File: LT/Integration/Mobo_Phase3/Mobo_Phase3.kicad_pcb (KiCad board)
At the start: 4 copper layers, 90.2 x 95.9 mm, 70 parts, among them J1 Bus, J2 Conn_Coaxial, J3 Conn_Coaxial, J4 Conn_Coaxial, J6 Conn_Coaxial, J7 Conn_Coaxial, Q1 2N5486, U1 BAP64Q

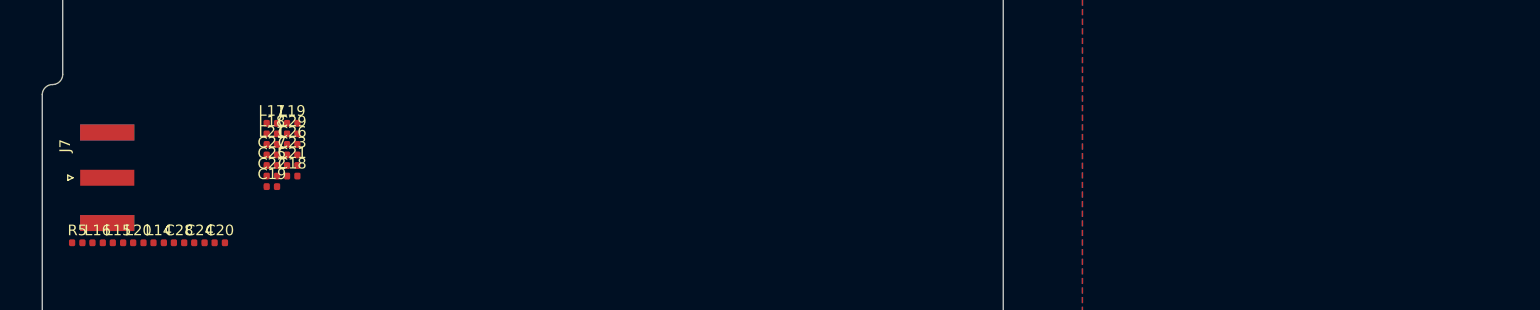
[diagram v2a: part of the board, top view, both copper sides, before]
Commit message: Finished PA Schematic Layout with footprints associated with it
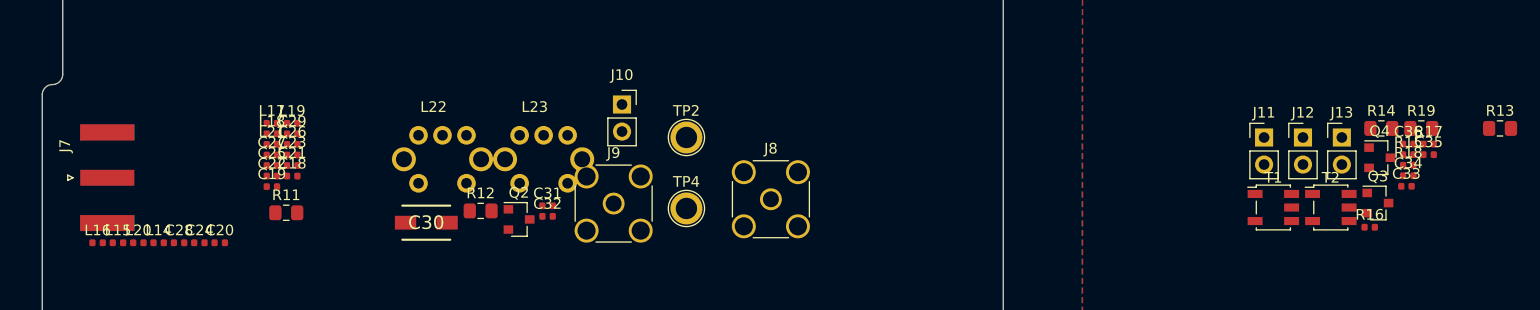
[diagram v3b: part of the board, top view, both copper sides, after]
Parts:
- removed R5: 0 Ohms, Resistor_SMD:R_0402_1005Metric
- added C30: C_Variable, LT:CAP_trimmer_SGC3_Download, F.Cu at (164.5, 107.6)
- added C31: 1uF, Capacitor_SMD:C_0402_1005Metric, F.Cu at (175.9, 106.0)
- added C32: 1uF, Capacitor_SMD:C_0402_1005Metric, F.Cu at (175.9, 107.0)
- added C33: 100nF, Capacitor_SMD:C_0402_1005Metric, F.Cu at (256.5, 104.2)
- added C34: 100nF, Capacitor_SMD:C_0402_1005Metric, F.Cu at (256.7, 103.2)
- added C35: 100nF, Capacitor_SMD:C_0402_1005Metric, F.Cu at (258.6, 101.2)
- added C36: 100nF, Capacitor_SMD:C_0402_1005Metric, F.Cu at (256.7, 100.2)
- added J10: Conn_01x02_Female, Connector_PinSocket_2.54mm:PinSocket_1x02_P2.54mm_Vertical, F.Cu at (182.9, 96.5)
- added J11: Conn_01x02_Male, Connector_PinHeader_2.54mm:PinHeader_1x02_P2.54mm_Vertical, F.Cu at (243.1, 99.6)
- added J12: Conn_01x02_Male, Connector_PinHeader_2.54mm:PinHeader_1x02_P2.54mm_Vertical, F.Cu at (246.8, 99.6)
- added J13: Conn_01x02_Male, Connector_PinHeader_2.54mm:PinHeader_1x02_P2.54mm_Vertical, F.Cu at (250.4, 99.6)
- added J8: Conn_Coaxial, Connector_Coaxial:SMA_Amphenol_132291_Vertical, F.Cu at (196.8, 105.4)
- added J9: Conn_Coaxial, Connector_Coaxial:SMA_Amphenol_132291_Vertical, F.Cu at (182.1, 105.8)
- added L22: LTRIM, LT:IND_trimmer_7M3, F.Cu at (166.0, 101.7)
- added L23: LTRIM, LT:IND_trimmer_7M3, F.Cu at (175.5, 101.7)
- added Q2: Q_NJFET_DSG, Package_TO_SOT_SMD:SOT-23, F.Cu at (173.2, 107.3)
- added Q3: Q_NPN_BEC, Package_TO_SOT_SMD:SOT-23, F.Cu at (253.8, 105.8)
- added Q4: Q_PNP_BEC, Package_TO_SOT_SMD:SOT-23, F.Cu at (254.0, 101.5)
- added R11: 0, Resistor_SMD:R_0805_2012Metric_Pad1.15x1.40mm_HandSolder, F.Cu at (151.4, 106.7)
- added R12: 0, Resistor_SMD:R_0805_2012Metric_Pad1.15x1.40mm_HandSolder, F.Cu at (169.6, 106.5)
- added R13: 0, Resistor_SMD:R_0805_2012Metric_Pad1.15x1.40mm_HandSolder, F.Cu at (265.3, 98.8)
- added R14: 0, Resistor_SMD:R_0805_2012Metric_Pad1.15x1.40mm_HandSolder, F.Cu at (254.1, 98.8)
- added R15: 33k, Resistor_SMD:R_0402_1005Metric, F.Cu at (256.7, 101.2)
- added R16: 47k, Resistor_SMD:R_0402_1005Metric, F.Cu at (253.0, 108.0)
- added R17: 33k, Resistor_SMD:R_0402_1005Metric, F.Cu at (258.6, 100.2)
- added R18: 47k, Resistor_SMD:R_0402_1005Metric, F.Cu at (256.7, 102.2)
- added R19: 0, Resistor_SMD:R_0805_2012Metric_Pad1.15x1.40mm_HandSolder, F.Cu at (257.9, 98.8)
- added T1: Transformer_1P_SS, Transformer_SMD:Transformer_MACOM_SM-22, F.Cu at (244.0, 106.2)
- added T2: Transformer_1P_SS, Transformer_SMD:Transformer_MACOM_SM-22, F.Cu at (249.4, 106.2)
- added TP2: TestPoint_Probe, TestPoint:TestPoint_Plated_Hole_D2.0mm, F.Cu at (188.9, 99.6)
- added TP4: TestPoint_Probe, TestPoint:TestPoint_Plated_Hole_D2.0mm, F.Cu at (188.9, 106.3)
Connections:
- net Net-(C18-Pad1) renamed /29.4 MHz Bandpass Filter/29.4BPF_IN
- C29 pad 1: Net-(C29-Pad1) -> /29.4 MHz Bandpass Filter/29.4BPF_OUT
- J1 pad 1: (no net) -> Net-(J1-Pad1)
- J1 pad 10: (no net) -> Net-(J1-Pad10)
- J1 pad 100: (no net) -> Net-(J1-Pad100)
- J1 pad 101: (no net) -> Net-(J1-Pad101)
- J1 pad 102: (no net) -> Net-(J1-Pad102)
- J1 pad 103: (no net) -> Net-(J1-Pad103)
- J1 pad 104: (no net) -> Net-(J1-Pad104)
- J1 pad 105: (no net) -> Net-(J1-Pad105)
- J1 pad 106: (no net) -> Net-(J1-Pad106)
- J1 pad 107: (no net) -> Net-(J1-Pad107)
- J1 pad 108: (no net) -> Net-(J1-Pad108)
- J1 pad 109: (no net) -> Net-(J1-Pad109)
- J1 pad 11: (no net) -> Net-(J1-Pad11)
- J1 pad 110: (no net) -> Net-(J1-Pad110)
- J1 pad 111: (no net) -> Net-(J1-Pad111)
- J1 pad 112: (no net) -> Net-(J1-Pad112)
- J1 pad 113: (no net) -> Net-(J1-Pad113)
- J1 pad 114: (no net) -> Net-(J1-Pad114)
- J1 pad 115: (no net) -> Net-(J1-Pad115)
- J1 pad 116: /Variable Attenuator/Control_Voltage_From_MicroController -> Net-(J1-Pad116)
- J1 pad 117: (no net) -> Net-(J1-Pad117)
- J1 pad 118: (no net) -> Net-(J1-Pad118)
- J1 pad 119: (no net) -> Net-(J1-Pad119)
- J1 pad 12: (no net) -> Net-(J1-Pad12)
- J1 pad 120: (no net) -> Net-(J1-Pad120)
- J1 pad 13: (no net) -> Net-(J1-Pad13)
- J1 pad 14: (no net) -> Net-(J1-Pad14)
- J1 pad 15: (no net) -> Net-(J1-Pad15)
- J1 pad 16: (no net) -> Net-(J1-Pad16)
- J1 pad 17: (no net) -> Net-(J1-Pad17)
- J1 pad 18: (no net) -> Net-(J1-Pad18)
- J1 pad 19: (no net) -> Net-(J1-Pad19)
- J1 pad 2: (no net) -> Net-(J1-Pad2)
- J1 pad 20: (no net) -> Net-(J1-Pad20)
- J1 pad 21: (no net) -> Net-(J1-Pad21)
- J1 pad 22: (no net) -> Net-(J1-Pad22)
- J1 pad 23: (no net) -> Net-(J1-Pad23)
- J1 pad 24: (no net) -> Net-(J1-Pad24)
- J1 pad 25: (no net) -> Net-(J1-Pad25)
- J1 pad 26: (no net) -> Net-(J1-Pad26)
- J1 pad 27: (no net) -> Net-(J1-Pad27)
- J1 pad 28: (no net) -> Net-(J1-Pad28)
- J1 pad 29: (no net) -> Net-(J1-Pad29)
- J1 pad 3: (no net) -> Net-(J1-Pad3)
- J1 pad 30: (no net) -> Net-(J1-Pad30)
- J1 pad 31: (no net) -> Net-(J1-Pad31)
- J1 pad 32: (no net) -> Net-(J1-Pad32)
- J1 pad 33: (no net) -> Net-(J1-Pad33)
- J1 pad 34: (no net) -> Net-(J1-Pad34)
- J1 pad 35: (no net) -> Net-(J1-Pad35)
- J1 pad 36: (no net) -> Net-(J1-Pad36)
- J1 pad 37: (no net) -> Net-(J1-Pad37)
- J1 pad 38: (no net) -> Net-(J1-Pad38)
- J1 pad 39: (no net) -> Net-(J1-Pad39)
- J1 pad 4: +5V -> Net-(J1-Pad4)
- J1 pad 40: (no net) -> Net-(J1-Pad40)
- J1 pad 41: (no net) -> Net-(J1-Pad41)
- J1 pad 42: (no net) -> Net-(J1-Pad42)
- J1 pad 43: (no net) -> Net-(J1-Pad43)
- J1 pad 44: (no net) -> Net-(J1-Pad44)
- J1 pad 45: (no net) -> Net-(J1-Pad45)
- J1 pad 46: (no net) -> Net-(J1-Pad46)
- J1 pad 47: (no net) -> Net-(J1-Pad47)
- J1 pad 48: (no net) -> Net-(J1-Pad48)
- J1 pad 49: (no net) -> Net-(J1-Pad49)
- J1 pad 5: (no net) -> Net-(J1-Pad5)
- J1 pad 50: (no net) -> Net-(J1-Pad50)
- J1 pad 51: (no net) -> Net-(J1-Pad51)
- J1 pad 52: (no net) -> Net-(J1-Pad52)
- J1 pad 53: (no net) -> Net-(J1-Pad53)
- J1 pad 54: (no net) -> Net-(J1-Pad54)
- J1 pad 55: (no net) -> Net-(J1-Pad55)
- J1 pad 56: (no net) -> Net-(J1-Pad56)
- J1 pad 57: (no net) -> Net-(J1-Pad57)
- J1 pad 58: (no net) -> Net-(J1-Pad58)
- J1 pad 59: (no net) -> Net-(J1-Pad59)
- J1 pad 6: (no net) -> Net-(J1-Pad6)
- J1 pad 60: (no net) -> Net-(J1-Pad60)
- J1 pad 61: (no net) -> Net-(J1-Pad61)
- J1 pad 62: (no net) -> Net-(J1-Pad62)
- J1 pad 63: (no net) -> Net-(J1-Pad63)
- J1 pad 64: (no net) -> Net-(J1-Pad64)
- J1 pad 65: (no net) -> Net-(J1-Pad65)
- J1 pad 66: (no net) -> Net-(J1-Pad66)
- J1 pad 67: (no net) -> Net-(J1-Pad67)
- J1 pad 68: (no net) -> Net-(J1-Pad68)
- J1 pad 69: (no net) -> Net-(J1-Pad69)
- J1 pad 7: (no net) -> Net-(J1-Pad7)
- J1 pad 70: (no net) -> Net-(J1-Pad70)
- J1 pad 71: (no net) -> Net-(J1-Pad71)
- J1 pad 72: (no net) -> Net-(J1-Pad72)
- J1 pad 73: (no net) -> Net-(J1-Pad73)
- J1 pad 74: (no net) -> Net-(J1-Pad74)
- J1 pad 75: (no net) -> Net-(J1-Pad75)
- J1 pad 76: (no net) -> Net-(J1-Pad76)
- J1 pad 77: (no net) -> Net-(J1-Pad77)
- J1 pad 78: (no net) -> Net-(J1-Pad78)
- J1 pad 79: (no net) -> Net-(J1-Pad79)
- J1 pad 8: (no net) -> Net-(J1-Pad8)
- J1 pad 80: (no net) -> Net-(J1-Pad80)
- J1 pad 81: (no net) -> Net-(J1-Pad81)
- J1 pad 82: (no net) -> Net-(J1-Pad82)
- J1 pad 83: (no net) -> Net-(J1-Pad83)
- J1 pad 84: (no net) -> Net-(J1-Pad84)
- J1 pad 85: (no net) -> Net-(J1-Pad85)
- J1 pad 86: (no net) -> Net-(J1-Pad86)
- J1 pad 87: (no net) -> Net-(J1-Pad87)
- J1 pad 88: (no net) -> Net-(J1-Pad88)
- J1 pad 89: (no net) -> Net-(J1-Pad89)
- J1 pad 9: (no net) -> Net-(J1-Pad9)
- J1 pad 90: (no net) -> Net-(J1-Pad90)
- J1 pad 91: (no net) -> Net-(J1-Pad91)
- J1 pad 92: (no net) -> Net-(J1-Pad92)
- J1 pad 93: (no net) -> Net-(J1-Pad93)
- J1 pad 94: (no net) -> Net-(J1-Pad94)
- J1 pad 95: (no net) -> Net-(J1-Pad95)
- J1 pad 96: (no net) -> Net-(J1-Pad96)
- J1 pad 97: (no net) -> Net-(J1-Pad97)
- J1 pad 98: (no net) -> Net-(J1-Pad98)
- J1 pad 99: (no net) -> Net-(J1-Pad99)
- L12 pad 3: GND -> (no net)
- L13 pad 2: GND -> Net-(C17-Pad2)
- L13 pad 3: Net-(C17-Pad2) -> (no net)
- Q1 pad 2: GND -> Net-(C15-Pad1)
- Q1 pad 3: Net-(C15-Pad1) -> GND
- R7 pad 2: (no net) -> /Image Reject Filter/Variable_Attenuator_Out
- R9 pad 2: (no net) -> /Low Noise Amplifier/Image_Reject_Out
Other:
- board text added: "PA "Step" Daughter Board"

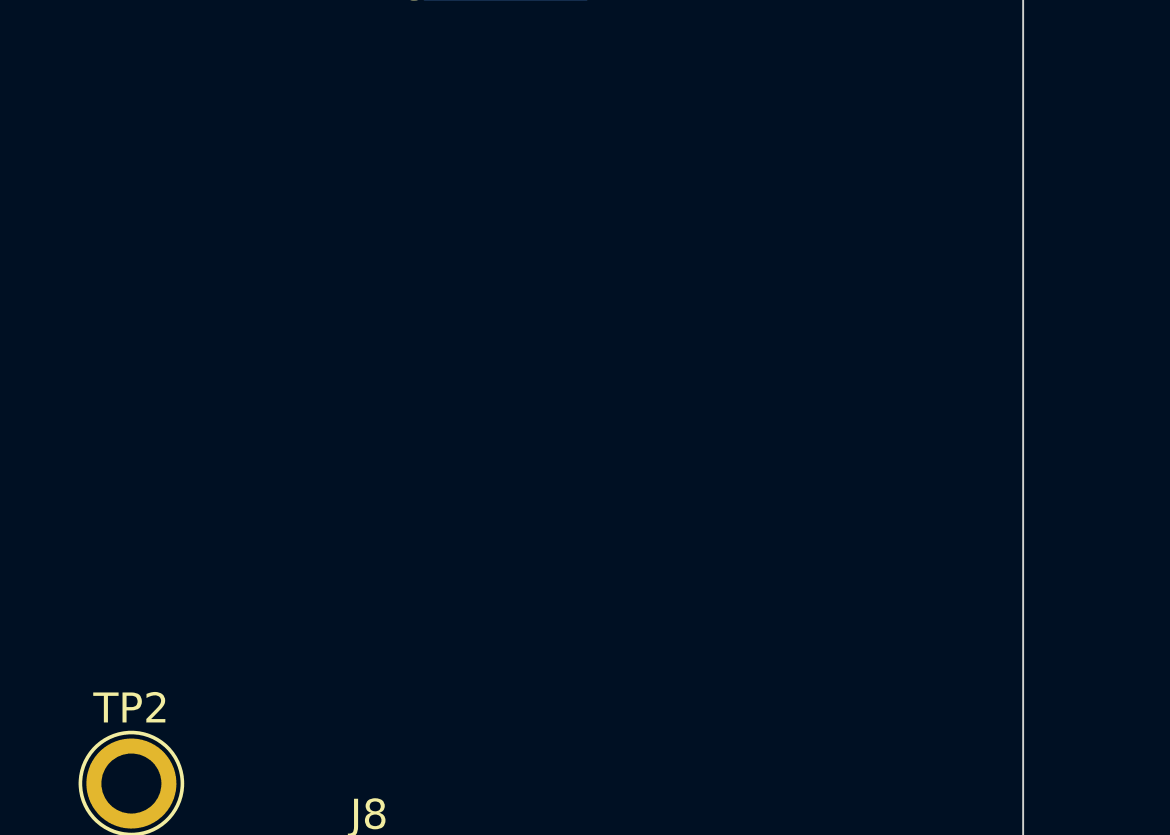
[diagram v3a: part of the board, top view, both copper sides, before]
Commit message: Finished 29.4 MHz LPF layout. PCB Layout of Transmitting Stage for Phase 3 is ready to be laid out
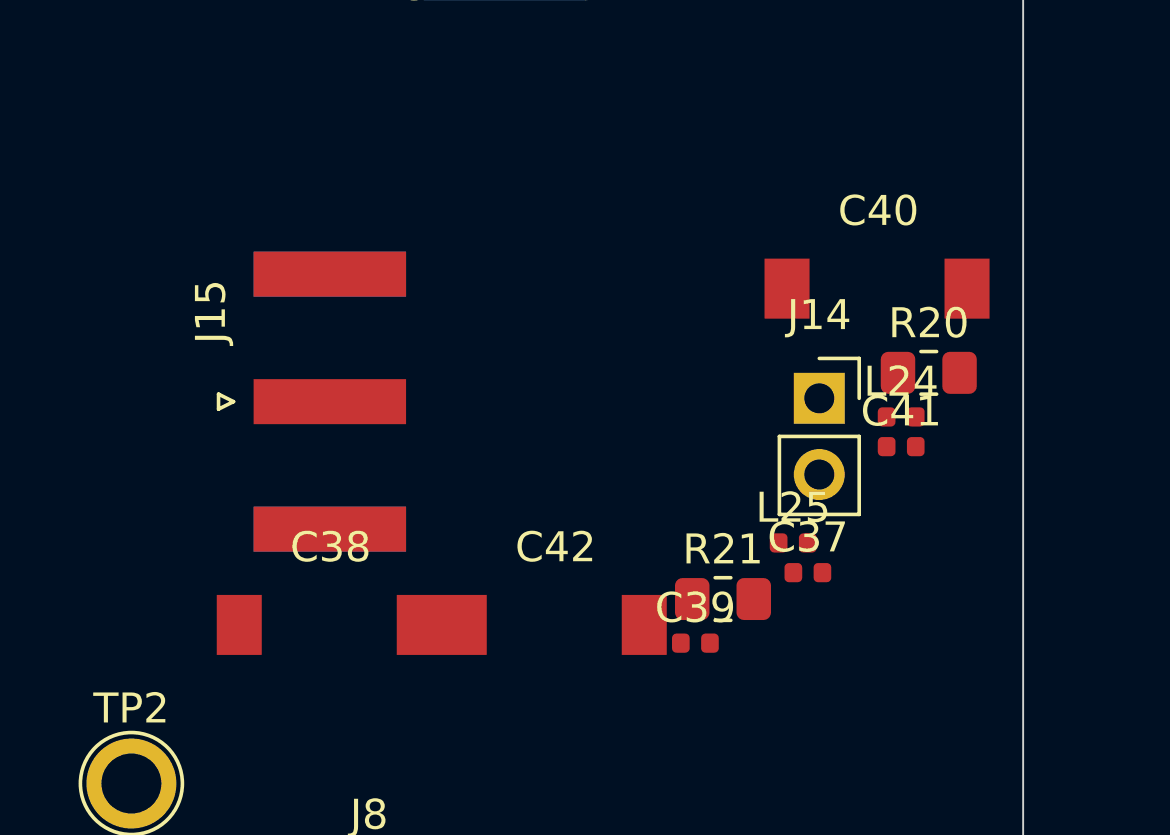
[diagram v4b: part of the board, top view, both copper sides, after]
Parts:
- added C37: 180pF, Capacitor_SMD:C_0402_1005Metric, F.Cu at (211.5, 92.6)
- added C38: C_Variable, LT:CAP_Trimmer_TZB4Z, F.Cu at (192.5, 94.3)
- added C39: 270pF, Capacitor_SMD:C_0402_1005Metric, F.Cu at (207.7, 94.9)
- added C40: C_Variable, LT:CAP_Trimmer_TZB4Z, F.Cu at (210.8, 83.1)
- added C41: 180pF, Capacitor_SMD:C_0402_1005Metric, F.Cu at (214.6, 88.4)
- added C42: C_Variable, LT:CAP_Trimmer_TZB4Z, F.Cu at (200.0, 94.3)
- added J14: Conn_01x02_Female, Connector_PinSocket_2.54mm:PinSocket_1x02_P2.54mm_Vertical, F.Cu at (211.9, 86.8)
- added J15: Conn_Coaxial, Connector_Coaxial:SMA_Amphenol_132289_EdgeMount, F.Cu at (195.5, 86.9)
- added L24: 330nH, Inductor_SMD:L_0402_1005Metric, F.Cu at (214.6, 87.4)
- added L25: 330nH, Inductor_SMD:L_0402_1005Metric, F.Cu at (211.0, 91.6)
- added R20: 0, Resistor_SMD:R_0805_2012Metric_Pad1.15x1.40mm_HandSolder, F.Cu at (215.5, 85.9)
- added R21: 0, Resistor_SMD:R_0805_2012Metric_Pad1.15x1.40mm_HandSolder, F.Cu at (208.6, 93.5)

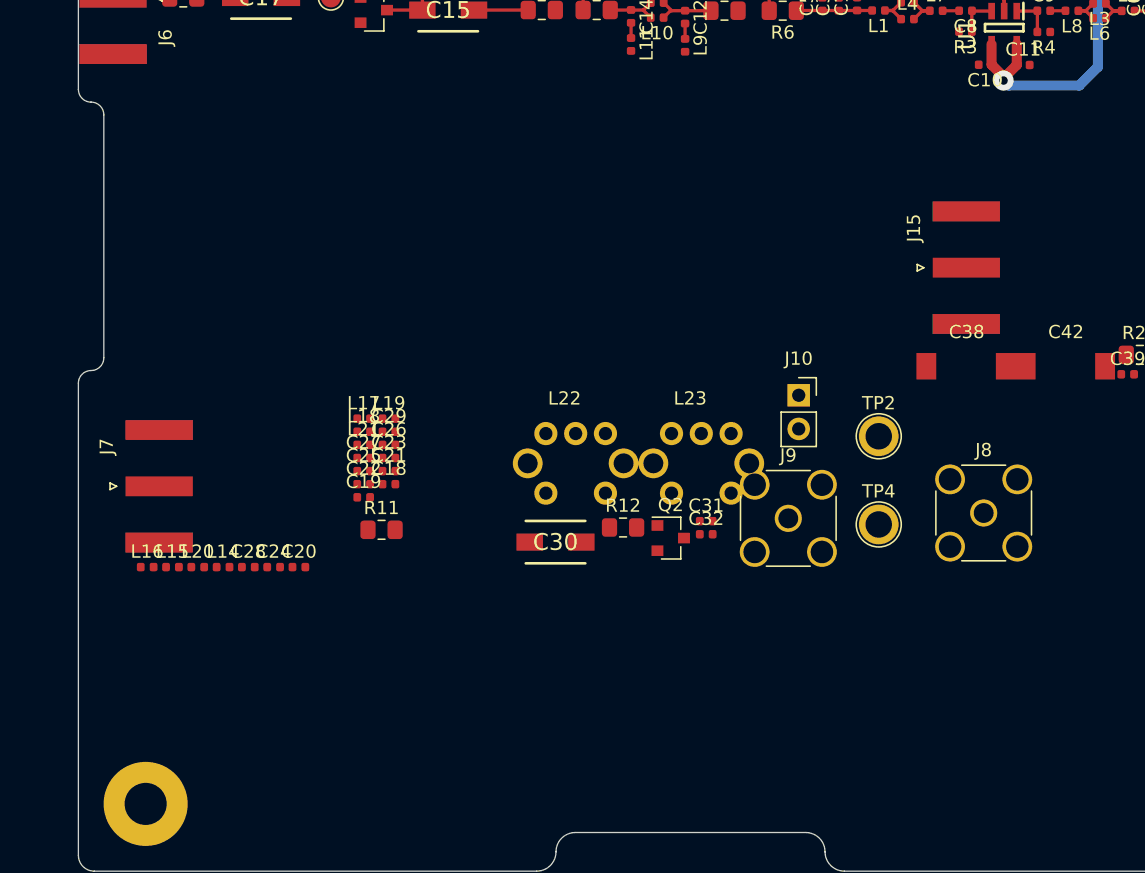
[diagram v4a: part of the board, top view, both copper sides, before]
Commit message: Finished 29.4 MHz BPF for Phase 3 of Transmitting Stage. 1/4 Completed
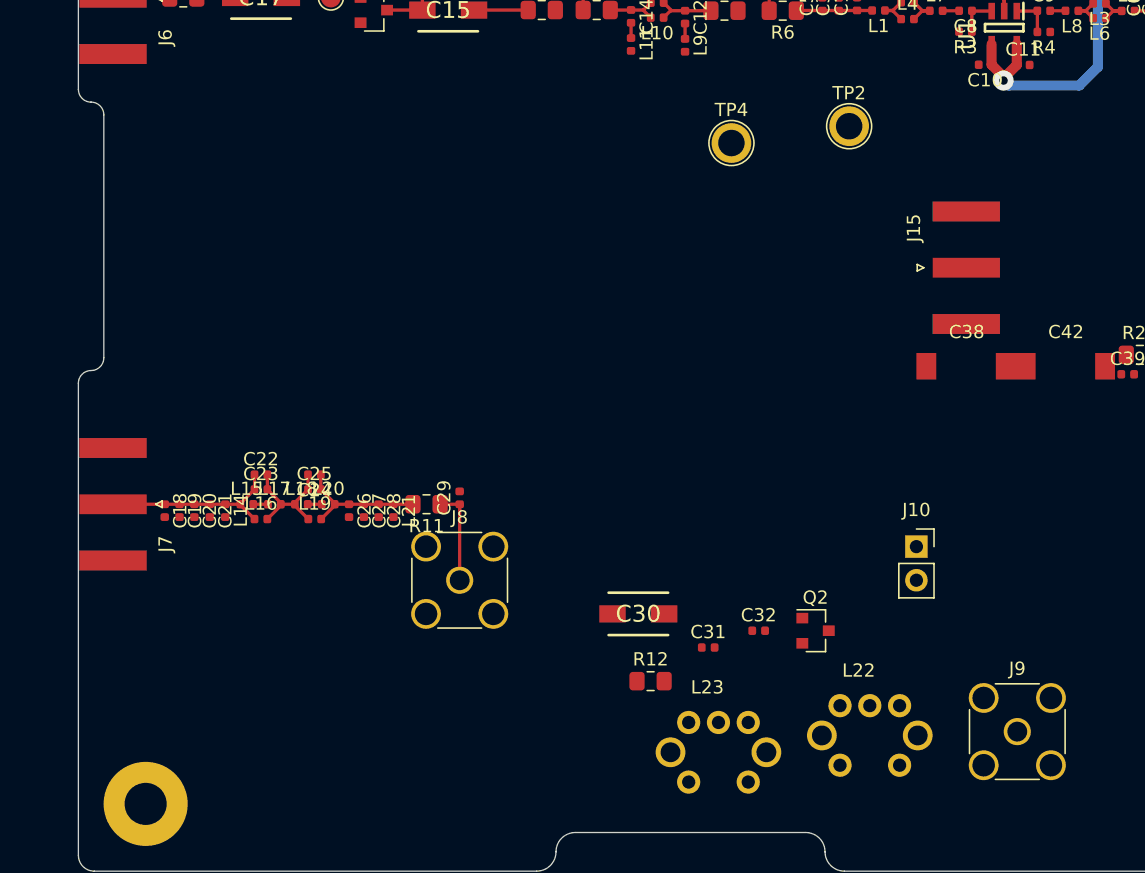
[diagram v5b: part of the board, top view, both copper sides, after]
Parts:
- moved J8 39.9 mm to (157.3, 110.5)
- moved TP4 30.9 mm to (177.8, 77.5)
- moved L22 30.3 mm to (188.2, 122.2)
- moved J9 23.6 mm to (199.4, 121.9)
- moved TP2 23.5 mm to (186.7, 76.2)
- moved L23 21.9 mm to (176.8, 123.5)
- moved C18 17.1 mm to (135.0, 105.2), turned to 270 degrees
- moved J10 14.5 mm to (191.8, 108.0)
- moved C19 13.9 mm to (136.1, 105.2), turned to 270 degrees
- moved C21 13.9 mm to (138.4, 105.2), turned to 270 degrees
- moved Q2 13.0 mm to (184.2, 114.3)
- moved R12 11.8 mm to (171.7, 118.1)
- moved L20 10.9 mm to (147.3, 104.7)
- moved C28 10.7 mm to (151.2, 105.2), turned to 270 degrees
- moved C23 9.96 mm to (142.3, 103.6)
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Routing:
- net /29.4 MHz Bandpass Filter/29.4BPF_IN: track 0.00 -> 14.0 mm
- net Net-(C24-Pad1): track 0.00 -> 10.1 mm
- net Net-(C22-Pad2): track 0.00 -> 9.62 mm
- net /29.4 MHz Bandpass Filter/29.4BPF_OUT: track 0.00 -> 7.22 mm
- net Net-(L15-Pad2): track 0.00 -> 1.11 mm
- net Net-(L18-Pad2): track 0.00 -> 1.06 mm
